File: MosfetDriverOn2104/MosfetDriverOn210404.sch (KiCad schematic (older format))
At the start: 88 parts, among them J1 I2C HDR, J10 ENCODER HDR, J11 CROSS CONN, J12 motor, J2 AVR-ISP-6, J3 I2C HDR, J4 Screw_Terminal_01x02, J5 I2C HDR, J6 UART HDR, J7 5V HDR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

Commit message: resistor footprint changed
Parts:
- R11, R12, R7, R8, R9: footprint Resistor_SMD:R_1206_3216Metric -> Resistor_SMD:R_2512_6332Metric
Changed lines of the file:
@@
 F 0 "R8" V 6400 -2950 50  0000 L CNN
 F 1 "0E05" V 6100 -2900 50  0001 L CNN
-F 2 "Resistor_SMD:R_1206_3216Metric" V 6330 -2850 50  0001 C CNN
+F 2 "Resistor_SMD:R_2512_6332Metric" V 6330 -2850 50  0001 C CNN
 F 3 "~" H 6400 -2850 50  0001 C CNN
 	1    6400 -2850
@@
 F 0 "R7" V 6300 -2950 50  0000 L CNN
 F 1 "0E05" V 6200 -2950 50  0000 L CNN
-F 2 "Resistor_SMD:R_1206_3216Metric" V 6230 -2850 50  0001 C CNN
+F 2 "Resistor_SMD:R_2512_6332Metric" V 6230 -2850 50  0001 C CNN
 F 3 "~" H 6300 -2850 50  0001 C CNN
 	1    6300 -2850
@@
 F 0 "R9" V 6500 -2950 50  0000 L CNN
 F 1 "0E05" V 6200 -2900 50  0001 L CNN
-F 2 "Resistor_SMD:R_1206_3216Metric" V 6430 -2850 50  0001 C CNN
+F 2 "Resistor_SMD:R_2512_6332Metric" V 6430 -2850 50  0001 C CNN
 F 3 "~" H 6500 -2850 50  0001 C CNN
 	1    6500 -2850
@@
 F 0 "R11" V 6600 -2950 50  0000 L CNN
 F 1 "0E05" V 6300 -2900 50  0001 L CNN
-F 2 "Resistor_SMD:R_1206_3216Metric" V 6530 -2850 50  0001 C CNN
+F 2 "Resistor_SMD:R_2512_6332Metric" V 6530 -2850 50  0001 C CNN
 F 3 "~" H 6600 -2850 50  0001 C CNN
 	1    6600 -2850
@@
 F 0 "R12" V 6700 -2950 50  0000 L CNN
 F 1 "0E05" V 6400 -2900 50  0001 L CNN
-F 2 "Resistor_SMD:R_1206_3216Metric" V 6630 -2850 50  0001 C CNN
+F 2 "Resistor_SMD:R_2512_6332Metric" V 6630 -2850 50  0001 C CNN
 F 3 "~" H 6700 -2850 50  0001 C CNN
 	1    6700 -2850

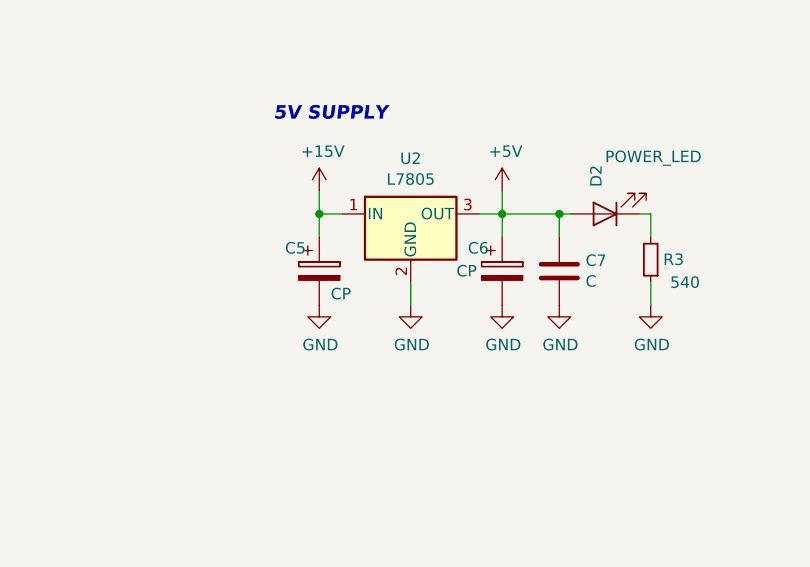
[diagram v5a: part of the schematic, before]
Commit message: Applying different packing strategy
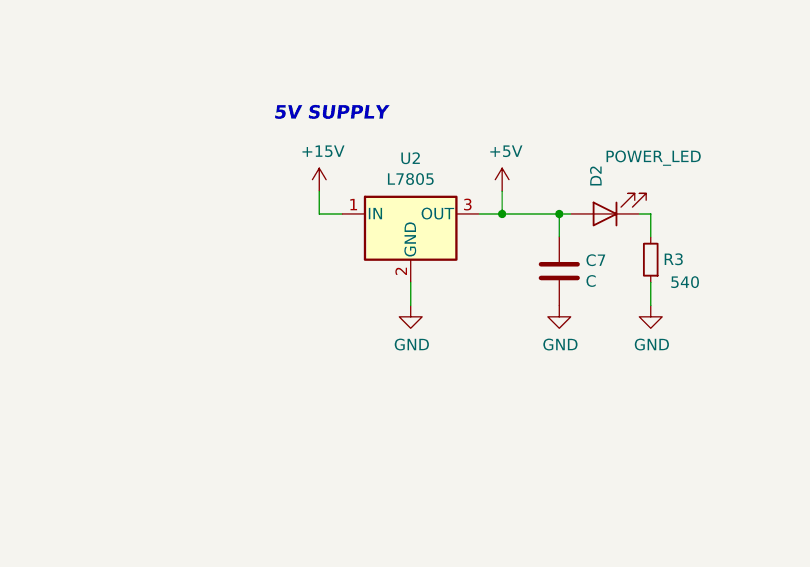
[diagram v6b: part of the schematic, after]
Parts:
- removed C5, C6: CP, Capacitor_SMD:CP_Elec_5x5.4, symbol Device:CP
- Q1, Q2, Q3, Q4: footprint Footprints:TO220_HS_SCREW -> TO220_HS_SCREW:TO220_HS_SCREW
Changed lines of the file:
@@
 Wire Wire Line
 	-1500 2550 -1600 2550
-$Comp
-L Device:CP C5
-U 1 1 5BD95B8D
-P -2300 2800
-AR Path="/5BD95B8D" Ref="C5"  Part="1"
-AR Path="/5BD0E604/5BD95B8D" Ref="C?"  Part="1"
-F 0 "C5" H -2450 2900 50  0000 L CNN
-F 1 "CP" H -2250 2700 50  0000 L CNN
-F 2 "Capacitor_SMD:CP_Elec_5x5.4" H -2262 2650 50  0001 C CNN
-F 3 "~" H -2300 2800 50  0001 C CNN
-	1    -2300 2800
-	1    0    0    -1
-$EndComp
-Wire Wire Line
-	-2300 2650 -2300 2550
-Connection ~ -2300 2550
-$Comp
-L power:GND #PWR0112
-U 1 1 5BD95B96
-P -2300 2950
-AR Path="/5BD95B96" Ref="#PWR0112"  Part="1"
-AR Path="/5BD0E604/5BD95B96" Ref="#PWR?"  Part="1"
-F 0 "#PWR0112" H -2300 2700 50  0001 C CNN
-F 1 "GND" H -2295 2777 50  0000 C CNN
-F 2 "" H -2300 2950 50  0001 C CNN
-F 3 "" H -2300 2950 50  0001 C CNN
-	1    -2300 2950
-	1    0    0    -1
-$EndComp
-$Comp
-L Device:CP C6
-U 1 1 5BD95B9C
-P -1500 2800
-AR Path="/5BD95B9C" Ref="C6"  Part="1"
-AR Path="/5BD0E604/5BD95B9C" Ref="C?"  Part="1"
-F 0 "C6" H -1650 2900 50  0000 L CNN
-F 1 "CP" H -1700 2800 50  0000 L CNN
-F 2 "Capacitor_SMD:CP_Elec_5x5.4" H -1462 2650 50  0001 C CNN
-F 3 "~" H -1500 2800 50  0001 C CNN
-	1    -1500 2800
-	1    0    0    -1
-$EndComp
-$Comp
-L power:GND #PWR0113
-U 1 1 5BD95BA3
-P -1500 2950
-AR Path="/5BD95BA3" Ref="#PWR0113"  Part="1"
-AR Path="/5BD0E604/5BD95BA3" Ref="#PWR?"  Part="1"
-F 0 "#PWR0113" H -1500 2700 50  0001 C CNN
-F 1 "GND" H -1495 2777 50  0000 C CNN
-F 2 "" H -1500 2950 50  0001 C CNN
-F 3 "" H -1500 2950 50  0001 C CNN
-	1    -1500 2950
-	1    0    0    -1
-$EndComp
-Wire Wire Line
-	-1500 2650 -1500 2550
 Connection ~ -1500 2550
 $Comp
@@
 F 0 "Q1" H 6050 -3750 50  0000 L CNN
 F 1 "IRF540N" V 6350 -4050 50  0000 L CNN
-F 2 "Footprints:TO220_HS_SCREW" H 6350 -3975 50  0001 L CIN
+F 2 "TO220_HS_SCREW:TO220_HS_SCREW" H 6350 -3975 50  0001 L CIN
 F 3 "http://www.irf.com/product-info/datasheets/data/irf540n.pdf" H 6100 -3900 50  0001 L CNN
 	1    6100 -3900
@@
 F 0 "Q2" H 6050 -3250 50  0000 L CNN
 F 1 "IRF540N" V 6350 -3550 50  0000 L CNN
-F 2 "Footprints:TO220_HS_SCREW" H 6350 -3475 50  0001 L CIN
+F 2 "TO220_HS_SCREW:TO220_HS_SCREW" H 6350 -3475 50  0001 L CIN
 F 3 "http://www.irf.com/product-info/datasheets/data/irf540n.pdf" H 6100 -3400 50  0001 L CNN
 	1    6100 -3400
@@
 F 0 "Q3" H 6800 -3750 50  0000 L CNN
 F 1 "IRF540N" V 7150 -4000 50  0000 L CNN
-F 2 "Footprints:TO220_HS_SCREW" H 7150 -3975 50  0001 L CIN
+F 2 "TO220_HS_SCREW:TO220_HS_SCREW" H 7150 -3975 50  0001 L CIN
 F 3 "http://www.irf.com/product-info/datasheets/data/irf540n.pdf" H 6900 -3900 50  0001 L CNN
 	1    6900 -3900
@@
 F 0 "Q4" H 6800 -3250 50  0000 L CNN
 F 1 "IRF540N" V 7150 -3550 50  0000 L CNN
-F 2 "Footprints:TO220_HS_SCREW" H 7150 -3475 50  0001 L CIN
+F 2 "TO220_HS_SCREW:TO220_HS_SCREW" H 7150 -3475 50  0001 L CIN
 F 3 "http://www.irf.com/product-info/datasheets/data/irf540n.pdf" H 6900 -3400 50  0001 L CNN
 	1    6900 -3400
@@
 P 19400 500
 AR Path="/5BCF2976/5BDA78C6" Ref="#PWR?"  Part="1"
-AR Path="/5BDA78C6" Ref="#PWR?"  Part="1"
-F 0 "#PWR?" H 19400 250 50  0001 C CNN
+AR Path="/5BDA78C6" Ref="#PWR0147"  Part="1"
+F 0 "#PWR0147" H 19400 250 50  0001 C CNN
 F 1 "GND" H 19405 327 50  0000 C CNN
 F 2 "" H 19400 500 50  0001 C CNN

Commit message: Almost moved everything in
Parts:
- C16: footprint Capacitor_SMD:CP_Elec_8x6.2 -> Capacitor_SMD:CP_Elec_10x7.9
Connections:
- net RX: now also J6.4 (Pin_4)
- net TX: now also J6.3 (Pin_3)
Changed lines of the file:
@@
 F 0 "C16" H -5032 2996 50  0000 L CNN
 F 1 "470" H -5032 2905 50  0000 L CNN
-F 2 "Capacitor_SMD:CP_Elec_8x6.2" H -5112 2800 50  0001 C CNN
+F 2 "Capacitor_SMD:CP_Elec_10x7.9" H -5112 2800 50  0001 C CNN
 F 3 "~" H -5150 2950 50  0001 C CNN
 	1    -5150 2950
@@
 	19400 200  19400 300
 Connection ~ 19400 300
+Wire Wire Line
+	-5900 -550 -6000 -550
+Wire Wire Line
+	-6000 -450 -5900 -450
 $EndSCHEMATC

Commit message: Routing done...
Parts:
- added J?: Conn_01x02_Female, Connector_PinHeader_2.54mm:PinHeader_1x02_P2.54mm_Vertical, symbol Connector:Conn_01x02_Female
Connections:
- net +15V: now also J?.2 (Pin_2)
- net SGN1: now also J11.4 (Pin_4), R23.2; no longer J11.1 (Pin_1)
- net SGN2: now also J11.1 (Pin_1), R24.2; no longer J11.4 (Pin_4)
- net VCC: now also J?.1 (Pin_1)
- net at D12.1 (K), R25.2, U6.13 ([9](OC1A)PB1): no longer R23.2
- net at D13.1 (K), R26.2, U6.14 ([10](OC1B/SS!)PB2): no longer R24.2
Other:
- moved on the sheet: C16, C4, D1, L1, R1, R2, R23, R24, U1
